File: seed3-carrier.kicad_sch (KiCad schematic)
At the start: 48 parts, among them J1 AudioJack2_Switch, J2 AudioJack2, J3 5V_IN, J4 DISPLAY_UART, J5 SJ1-3535NG, J6 Seed3_PINS_RIGHT, J7 Seed3_PINS_LEFT, Q1 AO3401A, U1 TLV9062IDR, U2 TPA6111A2DR

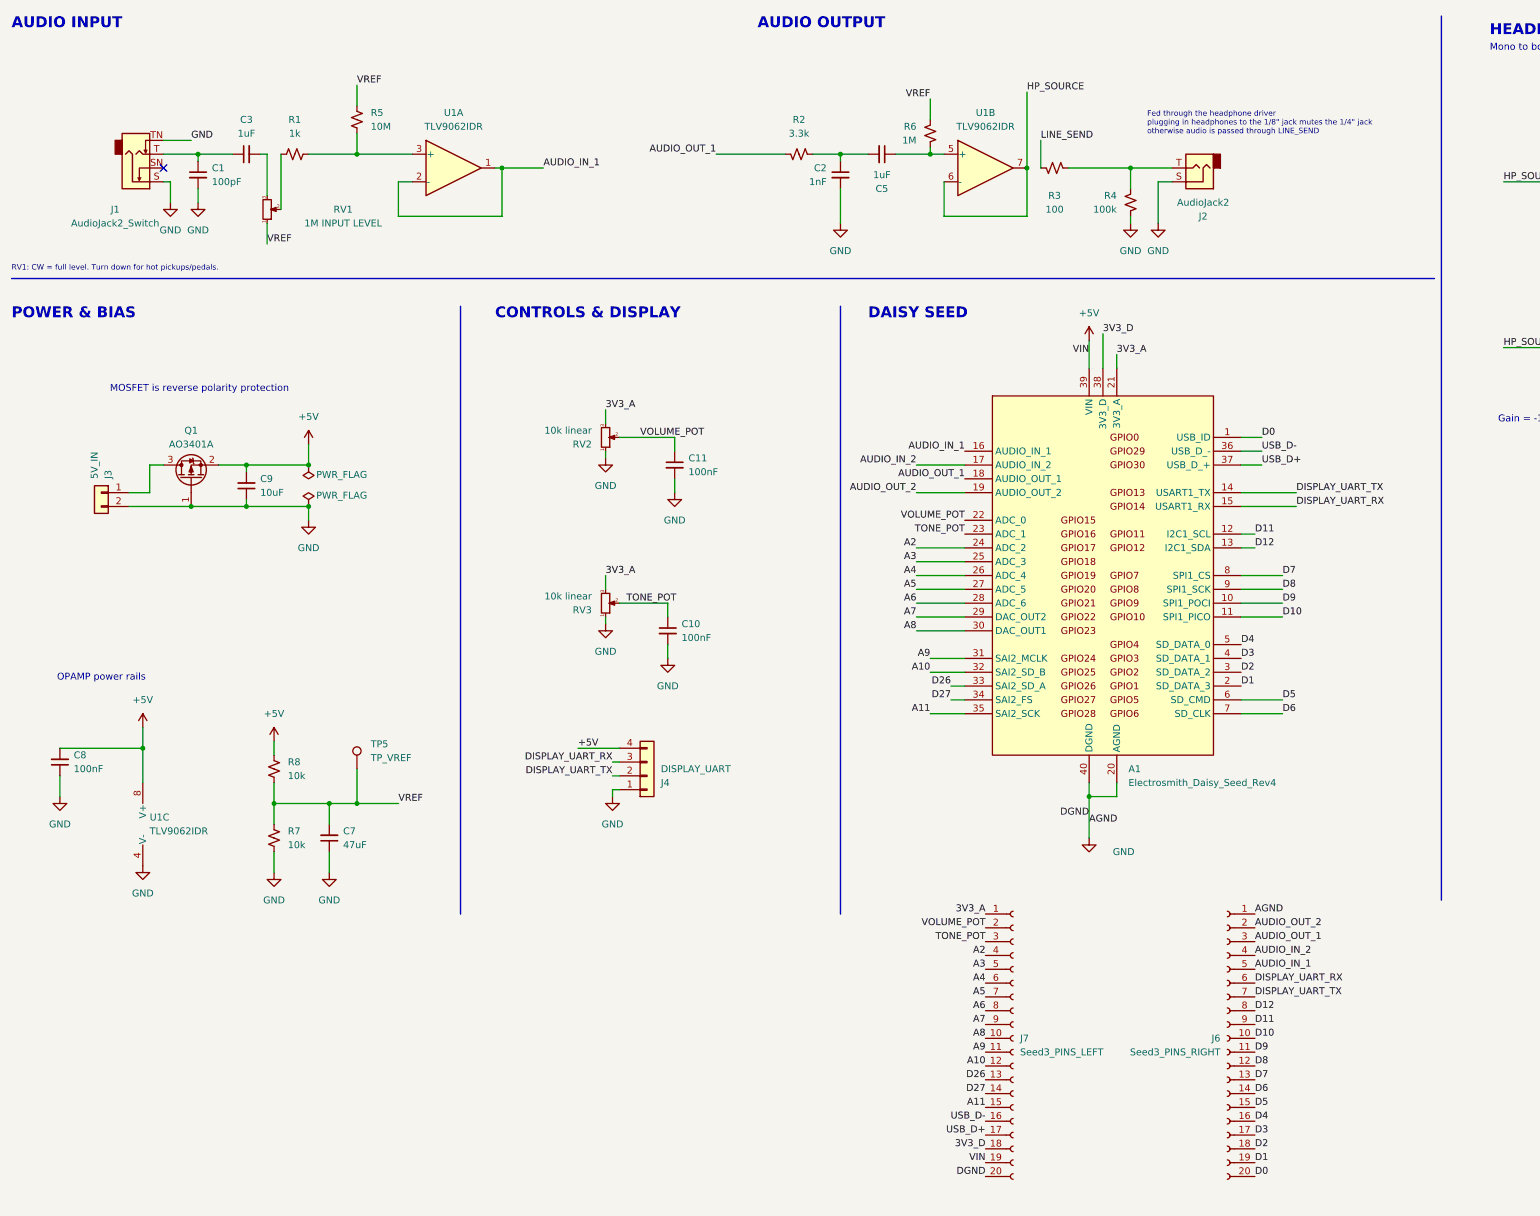
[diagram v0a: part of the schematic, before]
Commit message: Tidy schematic and clear ERC warnings
Remove redundant VIN/DGND/AGND labels at A1 and rename the breakout
header labels to +5V/GND. Add a heading for the Seed3 breakout headers
and extend the Daisy Seed section to enclose them. Move J1's text clear
of the adjacent GND symbol.

Co-Authored-By: Claude Opus 5.5 <noreply@anthropic.com>
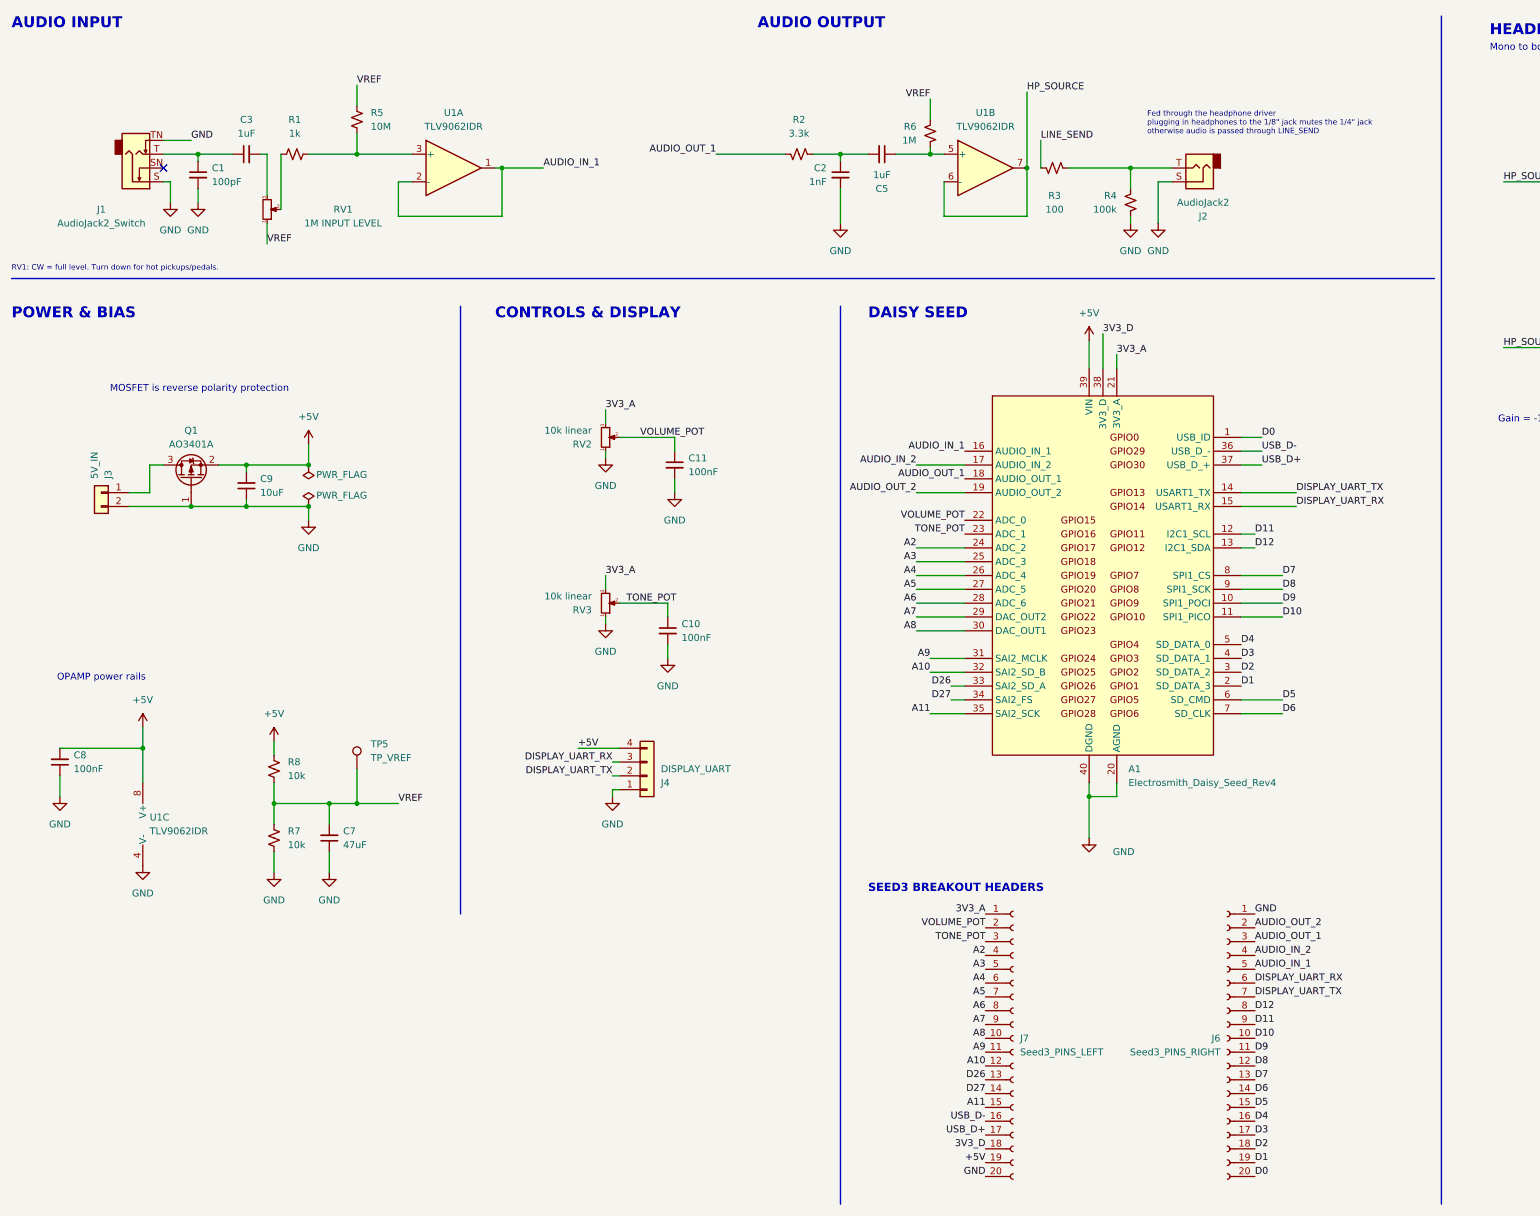
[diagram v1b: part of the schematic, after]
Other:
- note added: "SEED3 BREAKOUT HEADERS"
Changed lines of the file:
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@@
+		)
+	)
+	(text "SEED3 BREAKOUT HEADERS"
+		(exclude_from_sim no)
+		(at 175.26 176.53 0)
+		(effects
+			(font
+				(size 1.5 1.5)
+				(bold yes)
+			)
+			(justify left bottom)
 		)
 	)
@@
 	(polyline
 		(pts
-			(xy 170.18 68.58) (xy 170.18 180.34)
+			(xy 170.18 68.58) (xy 170.18 233.68)
 		)
 		(stroke
@@
 	(polyline
 		(pts
-			(xy 280.67 15.24) (xy 280.67 177.8)
+			(xy 280.67 15.24) (xy 280.67 233.68)
 		)
 		(stroke
@@
 		)
 	)
-	(label "VIN"
+	(label "+5V"
 		(at 196.85 226.06 180)
 		(effects
@@
 		)
 	)
-	(label "DGND"
-		(at 215.9 162.56 180)
-		(effects
-			(font
-				(size 1.27 1.27)
-			)
-			(justify right bottom)
-		)
-	)
 	(label "D4"
 		(at 243.84 130.81 0)
@@
 		)
 	)
-	(label "DGND"
+	(label "GND"
 		(at 196.85 228.6 180)
 		(effects
@@
 		)
 	)
-	(label "VIN"
-		(at 215.9 77.47 180)
-		(effects
-			(font
-				(size 1.27 1.27)
-			)
-			(justify right bottom)
-		)
-	)
 	(label "AUDIO_OUT_2"
 		(at 184.15 102.87 180)
@@
 		)
 	)
-	(label "AGND"
-		(at 215.9 163.83 0)
-		(effects
-			(font
-				(size 1.27 1.27)
-			)
-			(justify left bottom)
-		)
-	)
 	(label "USB_D+"
 		(at 247.65 97.79 0)
@@
 		)
 	)
-	(label "AGND"
+	(label "GND"
 		(at 246.38 180.34 0)
 		(effects
@@
 		(dnp no)
 		(property "Reference" "J1"
-			(at 36.83 50.8 0)
+			(at 34.29 50.8 0)
 			(show_name no)
 			(do_not_autoplace no)
@@
 		)
 		(property "Value" "AudioJack2_Switch"
-			(at 36.83 53.34 0)
+			(at 34.29 53.34 0)
 			(show_name no)
 			(do_not_autoplace no)

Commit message: Refine schematic text, power symbols and title block
Replace the GND/+5V labels on J1 and J4 with power symbols. Rewrite the
J2/J5 line-out note and move it beside J2. Put reference above value on
C5, J2, J4, RV2 and RV3, and align R13 with R14. Move the op-amp power
rail group up to even out Power & Bias spacing. Set title block date to
2026-09-28 and rev to 1.0.

Co-Authored-By: Claude Opus 5.5 <noreply@anthropic.com>
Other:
- note added: "Line out: J2 is fed from HP_L through J5's tip switch (LINE_SEND). Plugging headphones into J5 mutes J2."
- note removed: "Fed through the headphone driver plugging in headphones to the 1/8" jack mutes the 1/4" jack otherwise audio is passed through LINE_SEND"
- moved on the sheet: C7, C8, R7, R8, TP5, U1C
